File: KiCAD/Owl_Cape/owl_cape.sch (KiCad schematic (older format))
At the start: 1 part, among them J1 Conn_02x20_Odd_Even_MountingP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

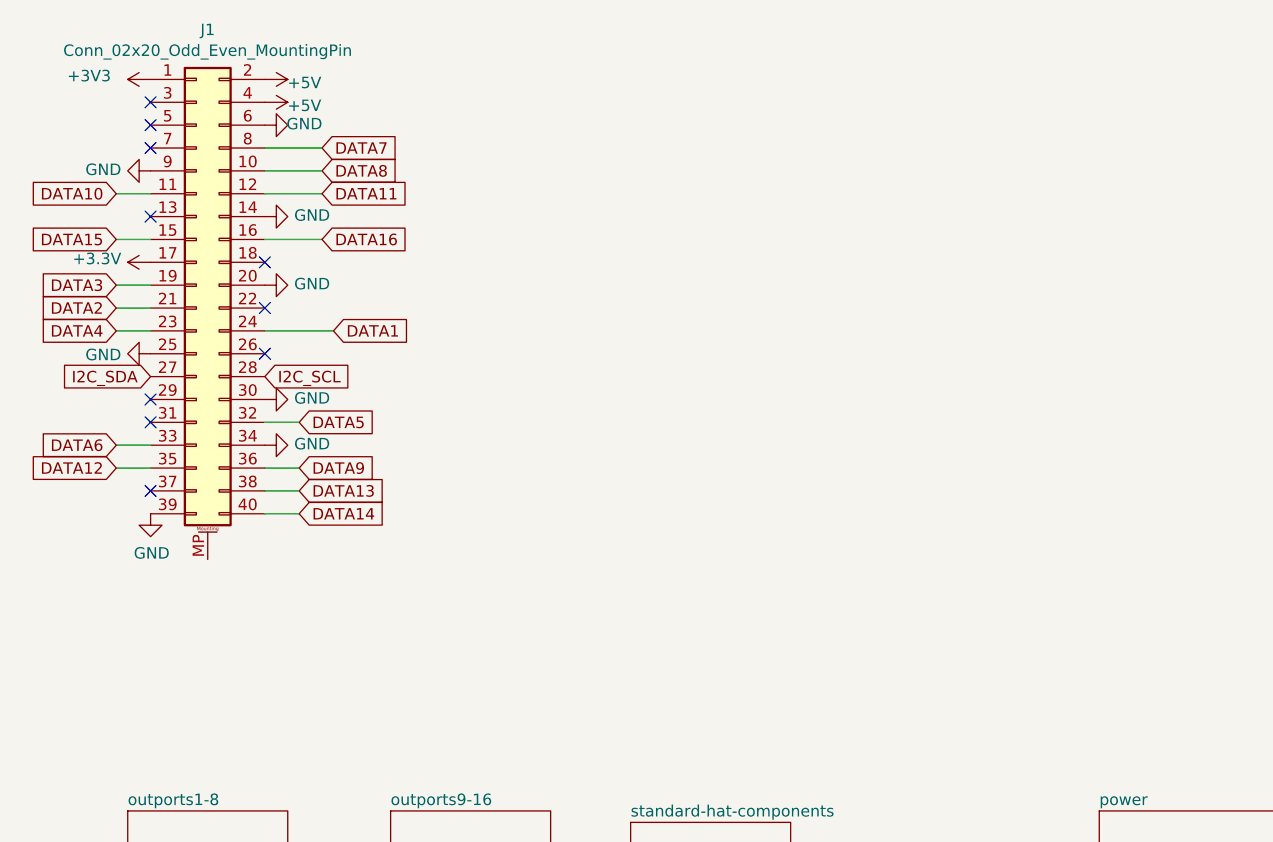
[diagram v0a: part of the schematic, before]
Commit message: logo and kicad updates
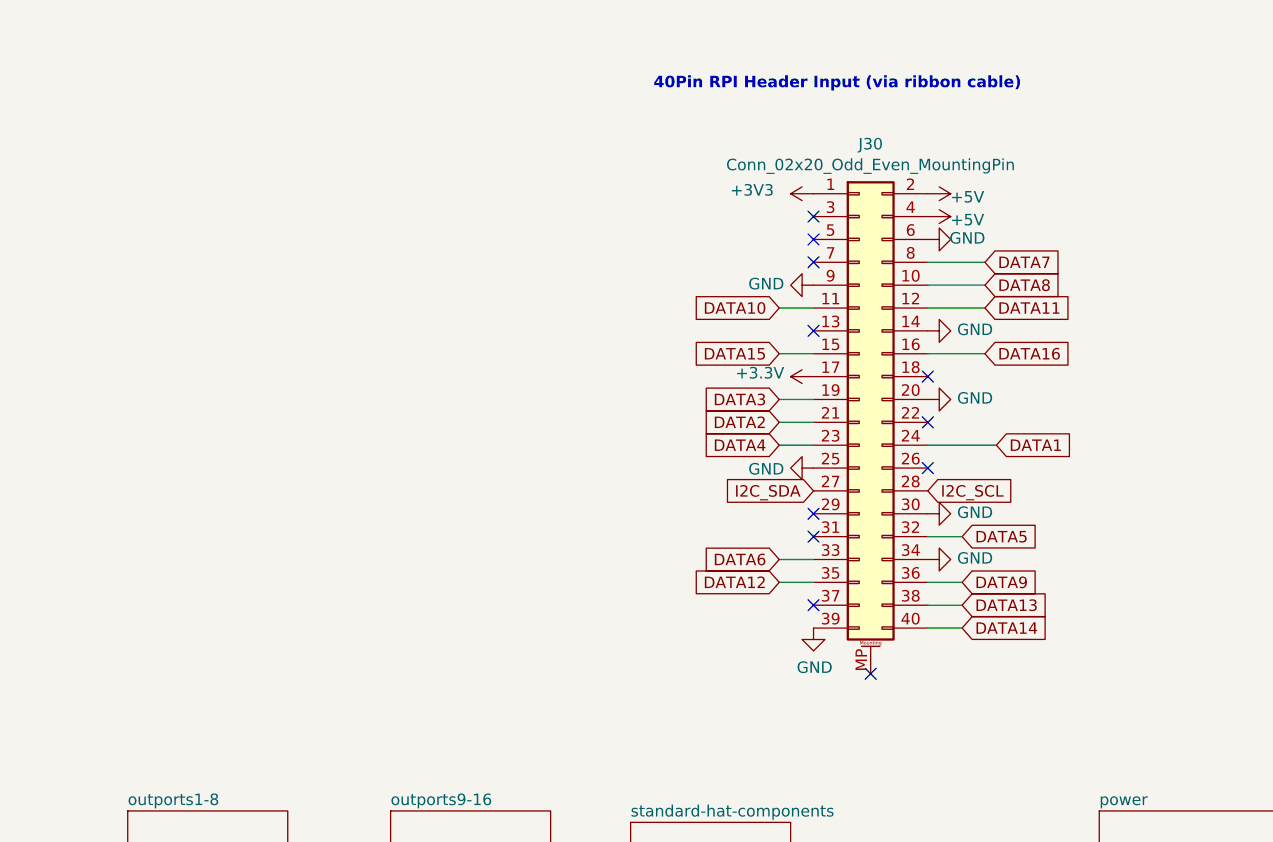
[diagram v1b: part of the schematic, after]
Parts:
- renumbered J1 to J30
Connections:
- no-connect marks 10 -> 11
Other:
- note added: "40Pin RPI Header Input (via ribbon cable)"
- moved on the sheet: J30

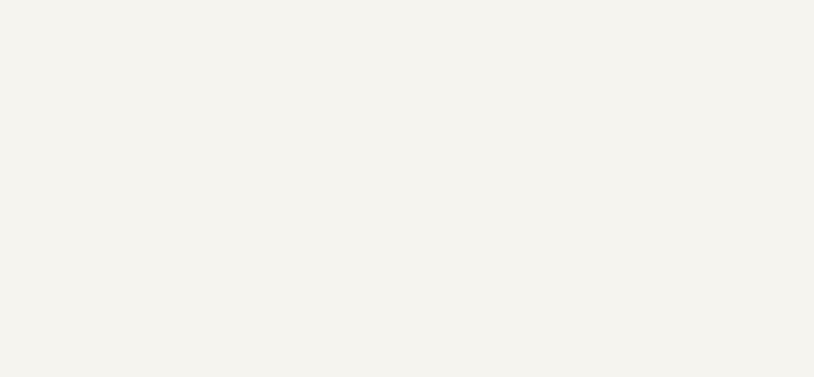
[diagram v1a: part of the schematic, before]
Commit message: updates and eeprom settings
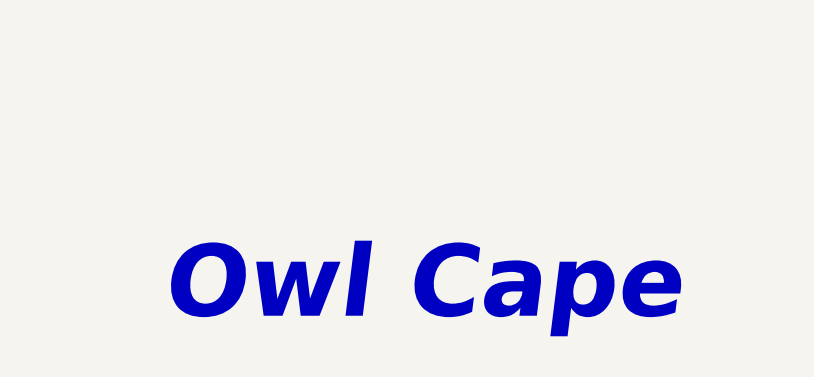
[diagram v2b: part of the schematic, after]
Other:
- note added: "Owl Cape"
